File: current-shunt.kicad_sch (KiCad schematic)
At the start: 25 parts, among them J4 Conn_01x02, U7 TSR_1-2450

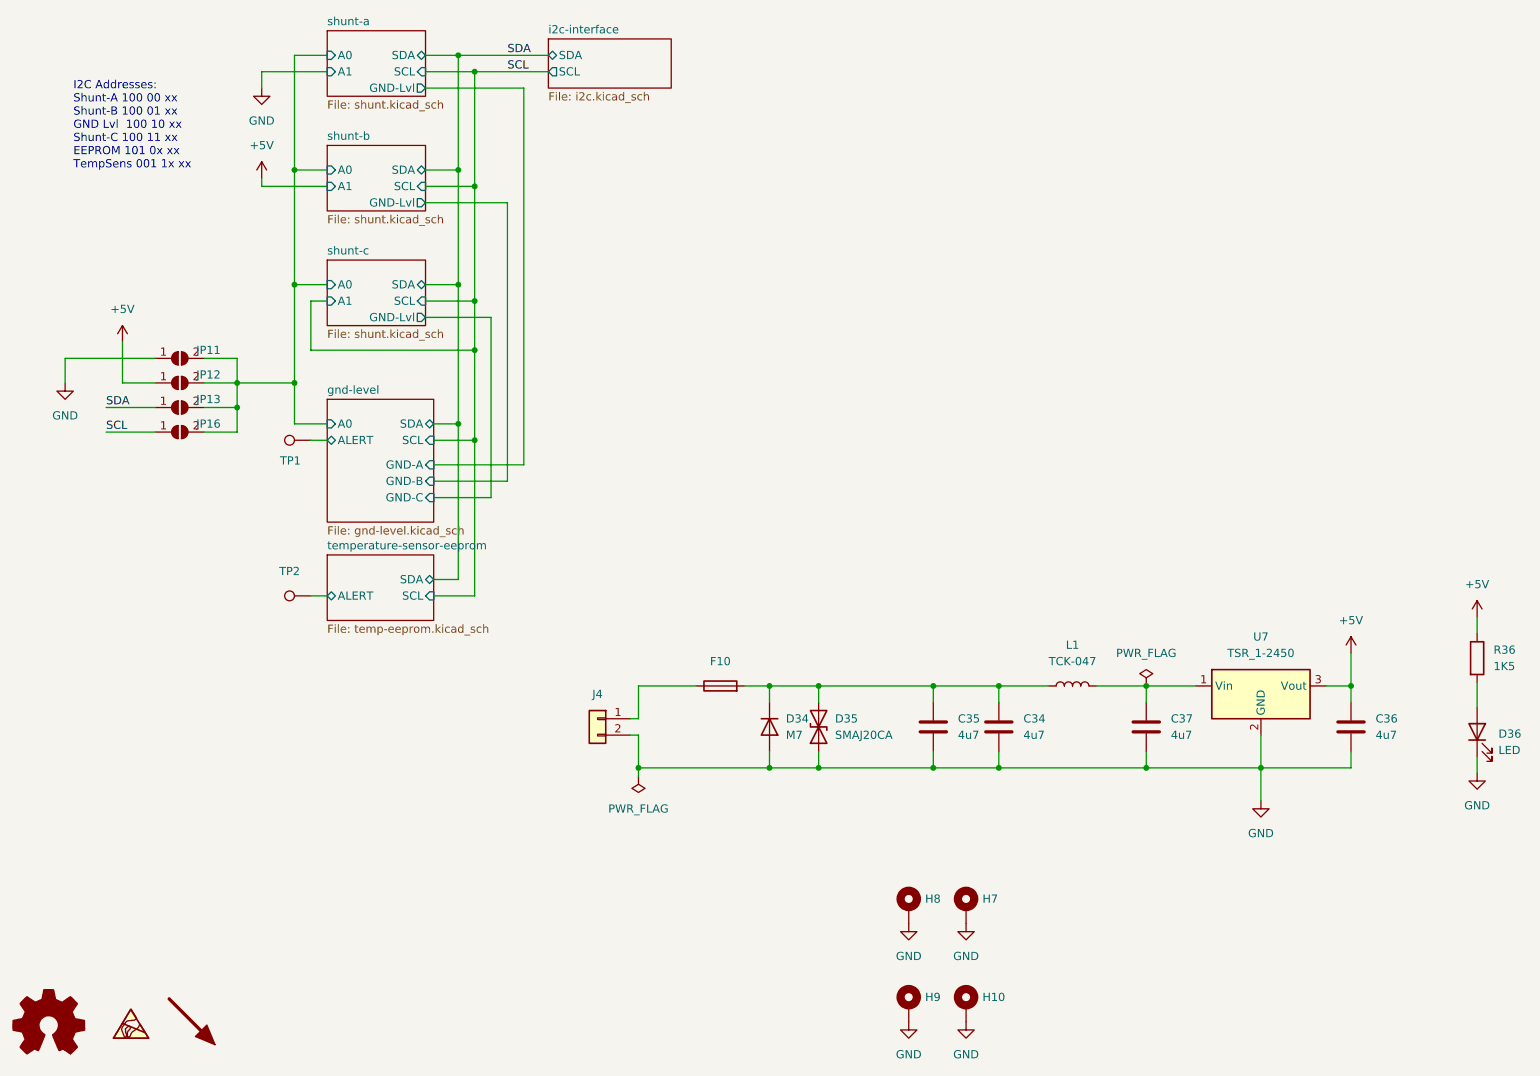
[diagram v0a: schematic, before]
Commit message: Shrink board and reduce features to reduce price
* Shrink to 100mm x 50mm
* Remove voltage regulator and use Stemma Power instead
* Remove isolation (is easier to add outside when needed)
* Remove reverse indicators to save space
* Remove I2C pullups as they are no longer needed
* Fix A2 of EEPROM and Temperature sensor to 0 to save space
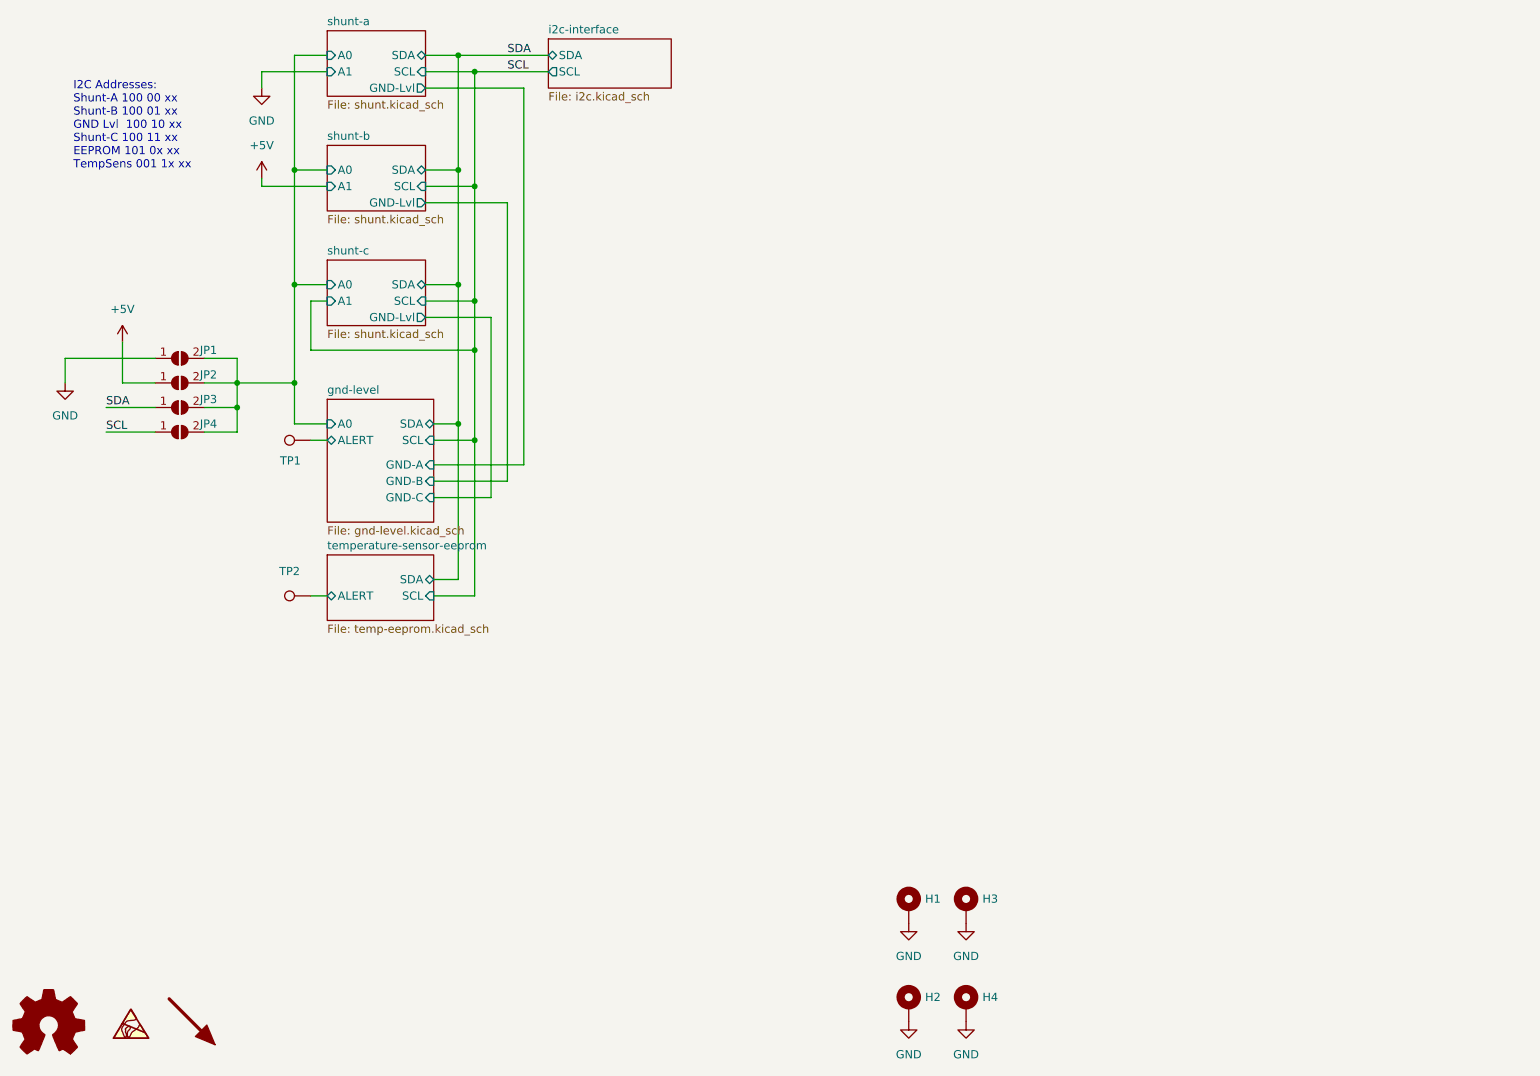
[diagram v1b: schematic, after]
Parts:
- removed C34, C35, C36, C37: 4u7, Capacitor_SMD:C_1206_3216Metric, symbol Device:C
- removed D34: M7, Diode_SMD:D_SMA, symbol Device:D
- removed D35: SMAJ20CA, Diode_SMD:D_SMA, symbol Device:D_TVS
- removed D36: LED, LED_SMD:LED_0603_1608Metric, symbol Device:LED
- removed F10: 1206L016WR, Fuse:Fuse_1206_3216Metric_Pad1.42x1.75mm_HandSolder, symbol Device:Fuse
- removed J4: Conn_01x02, TerminalBlock_MetzConnect:TerminalBlock_MetzConnect_Type094_RT03502HBLU_1x02_P5.00mm_Horizontal, symbol Connector_Generic:Conn_01x02
- removed L1: TCK-047, Inductor_SMD:L_TracoPower_TCK-047_5.2x5.8mm, symbol Device:L
- removed R36: 1K5, Resistor_SMD:R_0603_1608Metric, symbol Device:R
- removed U7: TSR_1-2450, Converter_DCDC:Converter_DCDC_TRACO_TSR-1_THT, symbol Regulator_Switching:TSR_1-2450
- renumbered H8 to H1, H9 to H2, H7 to H3, H10 to H4, JP11 to JP1, JP12 to JP2, JP13 to JP3, JP16 to JP4, LOGO3 to LOGO2, LOGO2 to LOGO3
